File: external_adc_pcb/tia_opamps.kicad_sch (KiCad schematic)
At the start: 46 parts, among them U18 TLV9064, U19 TLV9064, U20 TLV9064, U3 TLV9064

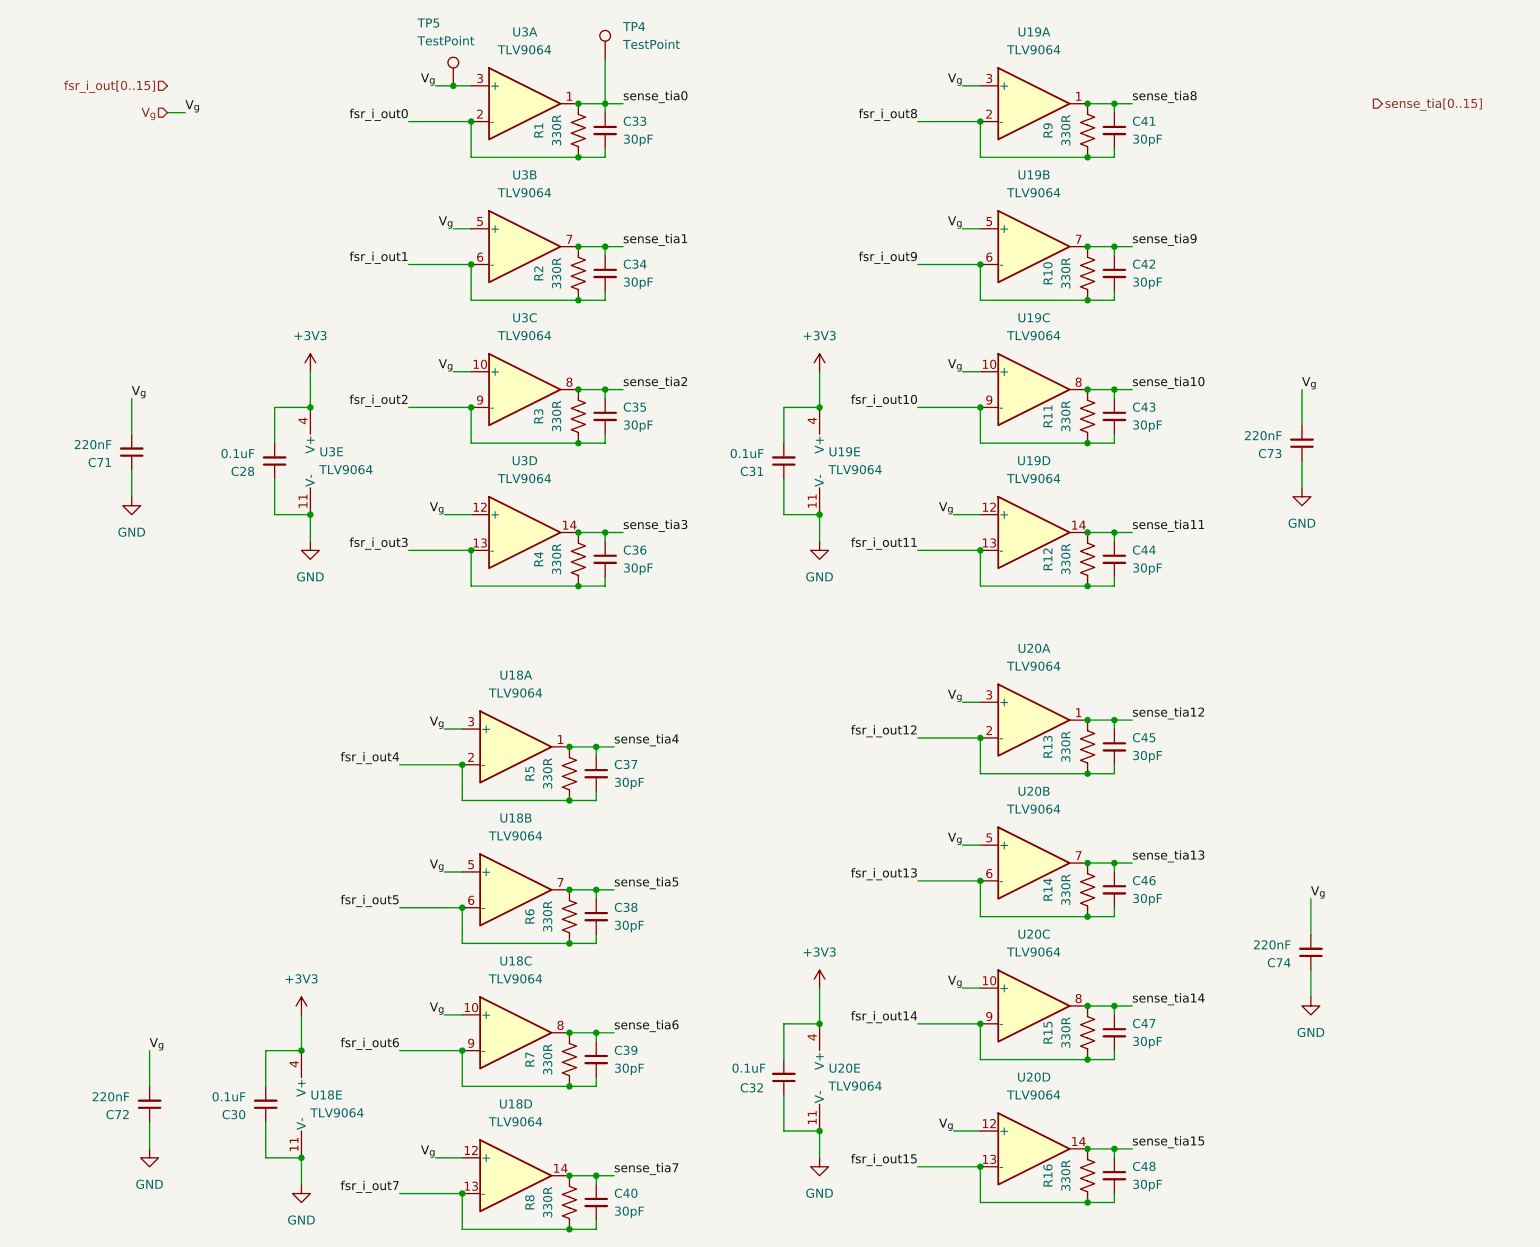
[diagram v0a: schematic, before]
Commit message: capitalize netnames; change and embed font
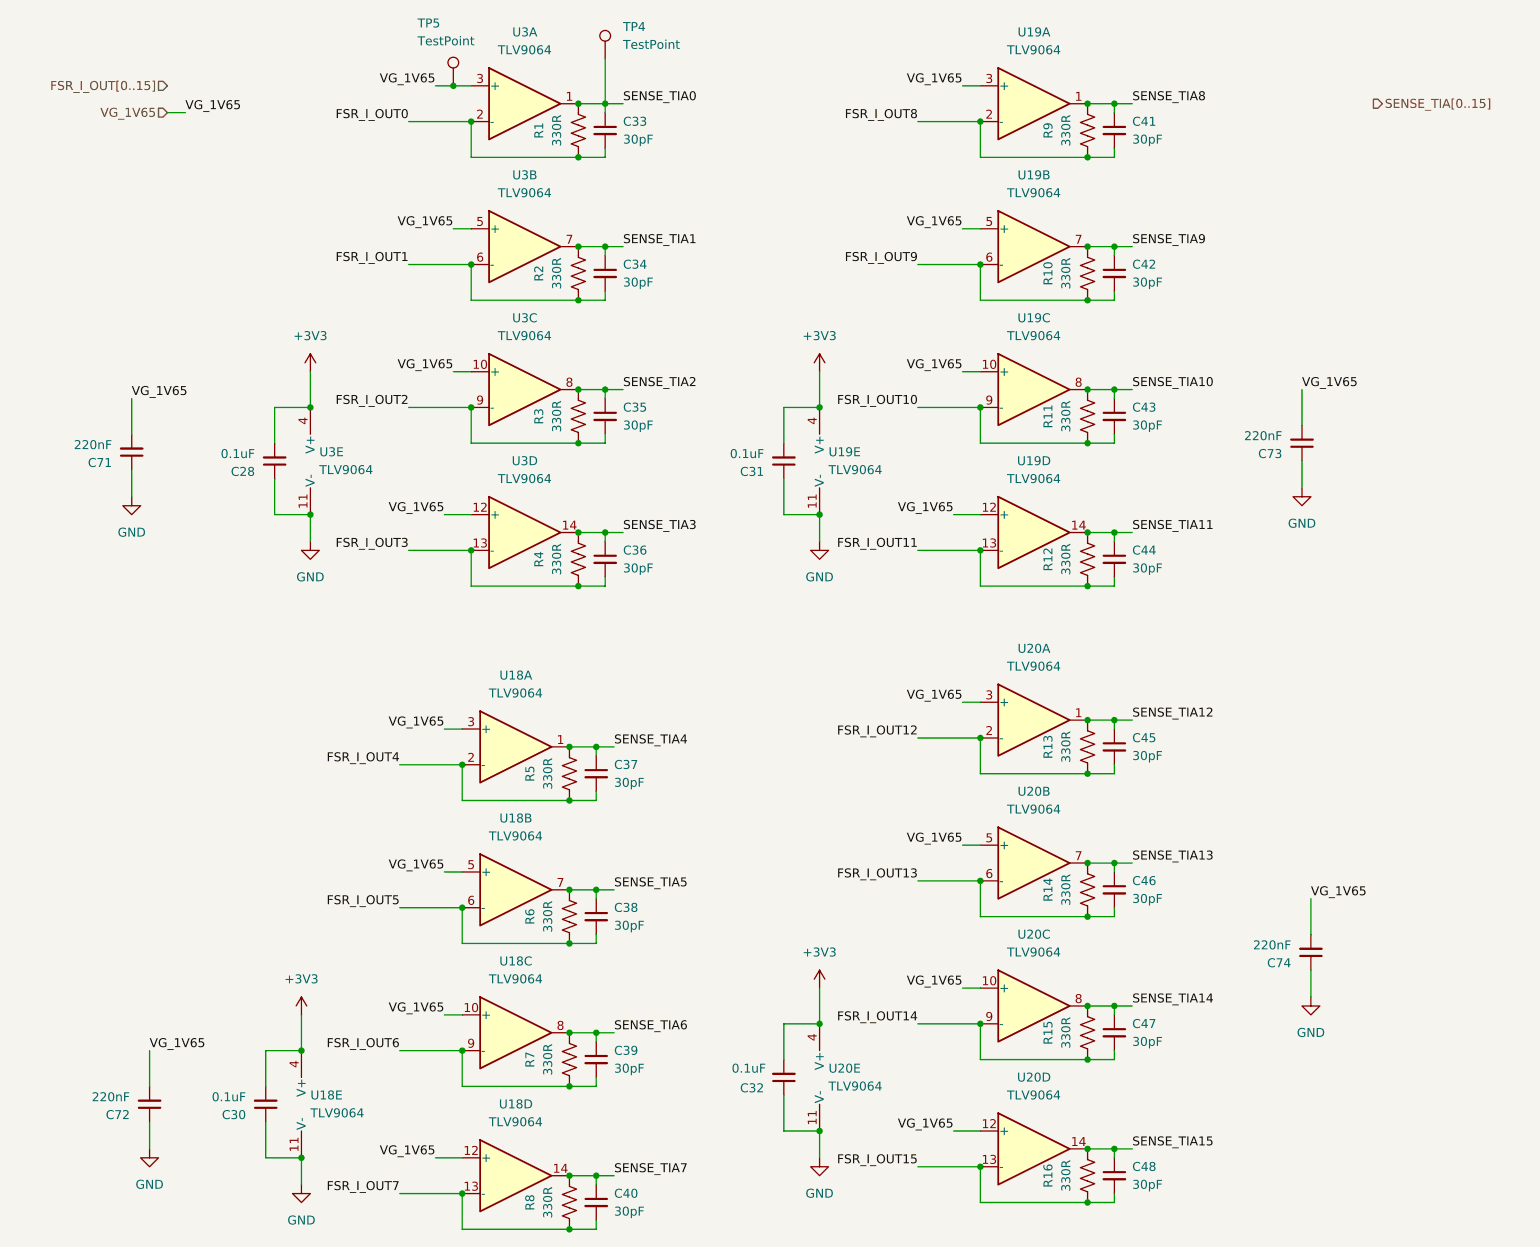
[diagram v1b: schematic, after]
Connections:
- net V_{g} renamed VG_1V65
- net fsr_i_out0 renamed FSR_I_OUT0
- net fsr_i_out1 renamed FSR_I_OUT1
- net fsr_i_out10 renamed FSR_I_OUT10
- net fsr_i_out11 renamed FSR_I_OUT11
- net fsr_i_out12 renamed FSR_I_OUT12
- net fsr_i_out13 renamed FSR_I_OUT13
- net fsr_i_out14 renamed FSR_I_OUT14
- net fsr_i_out15 renamed FSR_I_OUT15
- net fsr_i_out2 renamed FSR_I_OUT2
- net fsr_i_out3 renamed FSR_I_OUT3
- net fsr_i_out4 renamed FSR_I_OUT4
- net fsr_i_out5 renamed FSR_I_OUT5
- net fsr_i_out6 renamed FSR_I_OUT6
- net fsr_i_out7 renamed FSR_I_OUT7
- net fsr_i_out8 renamed FSR_I_OUT8
- net fsr_i_out9 renamed FSR_I_OUT9
- net sense_tia0 renamed SENSE_TIA0
- net sense_tia1 renamed SENSE_TIA1
- net sense_tia10 renamed SENSE_TIA10
- net sense_tia11 renamed SENSE_TIA11
- net sense_tia12 renamed SENSE_TIA12
- net sense_tia13 renamed SENSE_TIA13
- net sense_tia14 renamed SENSE_TIA14
- net sense_tia15 renamed SENSE_TIA15
- net sense_tia2 renamed SENSE_TIA2
- net sense_tia3 renamed SENSE_TIA3
- net sense_tia4 renamed SENSE_TIA4
- net sense_tia5 renamed SENSE_TIA5
- net sense_tia6 renamed SENSE_TIA6
- net sense_tia7 renamed SENSE_TIA7
- net sense_tia8 renamed SENSE_TIA8
- net sense_tia9 renamed SENSE_TIA9
